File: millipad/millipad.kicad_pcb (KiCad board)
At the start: 2 copper layers, 131.8 x 63.5 mm, 52 parts, among them SW1 SW_Push, SW2 Rotary_Encoder_Switch, U1 ATmega32U4-AU, U2 PRTR5V0U2X, Y1 16MHz

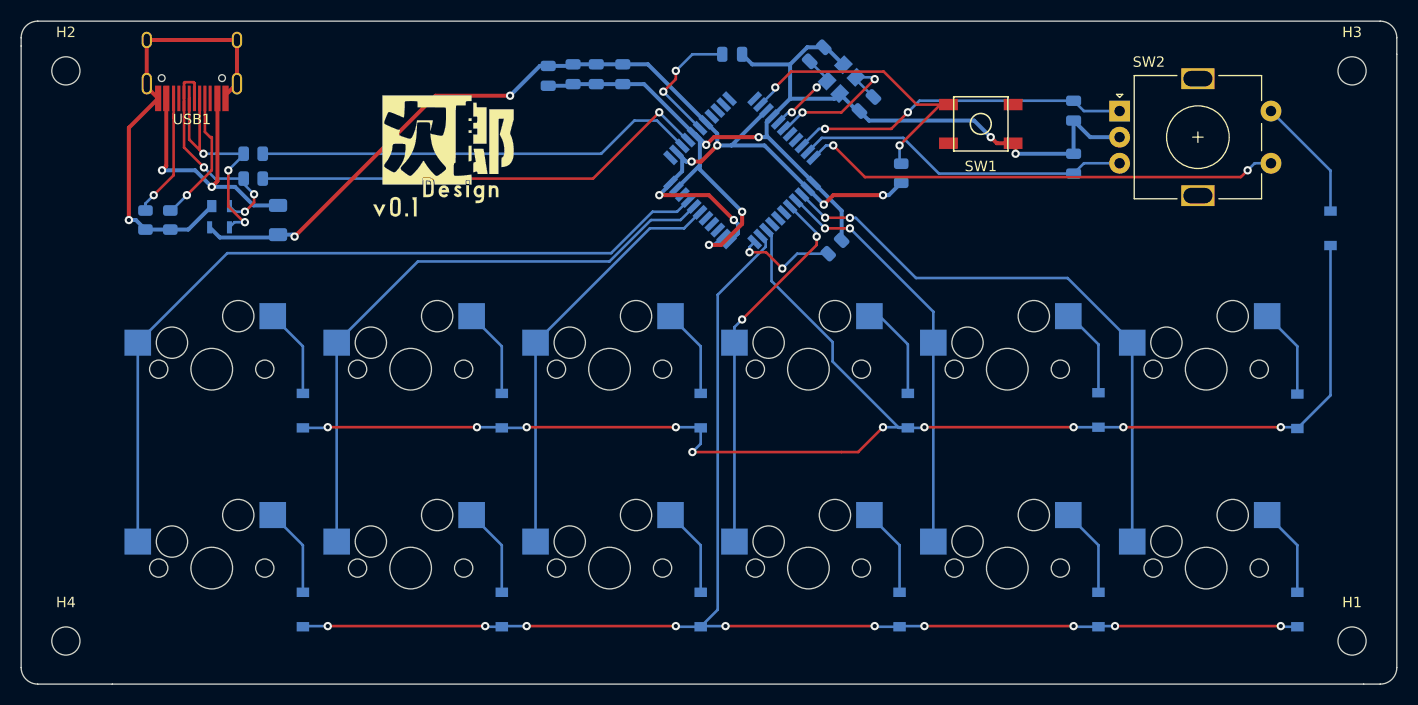
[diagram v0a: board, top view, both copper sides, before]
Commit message: OLED Implementation WIP
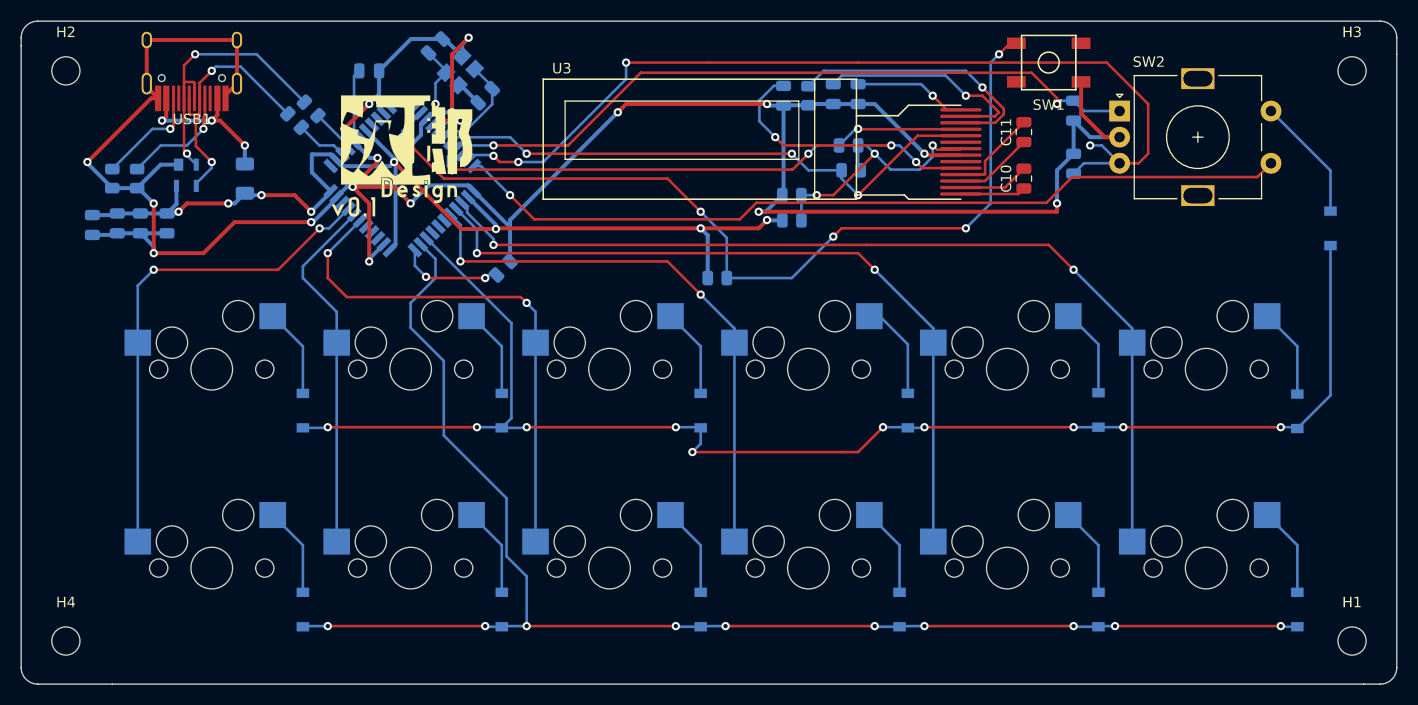
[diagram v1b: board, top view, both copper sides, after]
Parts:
- added C10: 1uF, Capacitor_SMD:C_0805_2012Metric, F.Cu at (166.7, 54.8)
- added C11: 1uF, Capacitor_SMD:C_0805_2012Metric, F.Cu at (166.7, 50.3)
- added C12: 1uF, Capacitor_SMD:C_0805_2012Metric, B.Cu at (143.7, 46.8)
- added C13: 4.7uF, Capacitor_SMD:C_0805_2012Metric, B.Cu at (148.4, 46.7)
- added C14: 2.2uF, Capacitor_SMD:C_0805_2012Metric, B.Cu at (150.8, 46.7)
- added R10: 2k, Resistor_SMD:R_0805_2012Metric, B.Cu at (150.1, 54.0)
- added R11: 2k, Resistor_SMD:R_0805_2012Metric, B.Cu at (149.9, 51.6)
- added R7: 1k, Resistor_SMD:R_0805_2012Metric, B.Cu at (144.5, 58.8)
- added R8: 2k, Resistor_SMD:R_0805_2012Metric, B.Cu at (144.5, 56.4)
- added R9: 330k, Resistor_SMD:R_0805_2012Metric, B.Cu at (146.1, 46.8)
- added U3: SSD1306, KiCad-SSD1306_OLED-0.91-128x32:SSD1306_OLED-0.91-128x32, F.Cu at (120.7, 45.2)
- moved C6 45.9 mm to (84.6, 59.1)
- moved C1 45.9 mm to (77.5, 59.2)
- moved C2 45.9 mm to (79.9, 59.1)
- moved C3 45.9 mm to (82.1, 59.1)
- moved C5 36.5 mm to (110.3, 42.1)
- moved C4 36.5 mm to (115.1, 46.8)
- moved Y1 36.5 mm to (112.7, 44.5)
- moved C7 34.8 mm to (104.0, 44.5)
- moved U1 32.6 mm to (107.2, 54.8)
- moved R4 31.8 mm to (116.8, 63.4)
- moved R3 20.3 mm to (137.3, 64.3), turned to 0 degrees
- moved SW1 8.77 mm to (169.1, 43.7)
- moved R2 8.69 mm to (98.4, 48.1), turned to 135 degrees
- moved R6 5.08 mm to (81.8, 54.8)
- moved R1 5.08 mm to (96.8, 49.2), turned to 135 degrees
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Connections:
- U1 pad 18: Net-(U1-Pad18) -> SCL
- U1 pad 19: Net-(U1-Pad19) -> SDA
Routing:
- net GND: track 157.0 -> 266.5 mm, vias 7 -> 17
- net Net-(R3-Pad2): track 28.9 -> 86.9 mm, vias 2 -> 5
- net ENC_B: track 32.2 -> 88.4 mm, vias 0 -> 4
- net SCL: track 0.00 -> 54.2 mm, vias 0 -> 3
- net SDA: track 0.00 -> 53.0 mm, vias 0 -> 3
- net Net-(R2-Pad1): track 44.5 -> 4.35 mm, vias 2 -> 0
- net Net-(R1-Pad1): track 42.5 -> 5.01 mm
- net ENC_A: track 32.6 -> 68.3 mm
- net COL6: track 46.1 -> 80.7 mm, vias 2 -> 1
- net COL5: track 56.6 -> 90.2 mm
- net COL4: track 39.6 -> 72.2 mm
- net COL0: track 77.4 -> 47.7 mm, vias 0 -> 2
- net +3V3: track 0.00 -> 26.2 mm, vias 0 -> 3
- net Net-(C12-Pad1): track 0.00 -> 26.0 mm, vias 0 -> 3
- net Net-(R9-Pad1): track 0.00 -> 25.8 mm, vias 0 -> 1
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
